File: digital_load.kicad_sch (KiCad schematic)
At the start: 0 parts

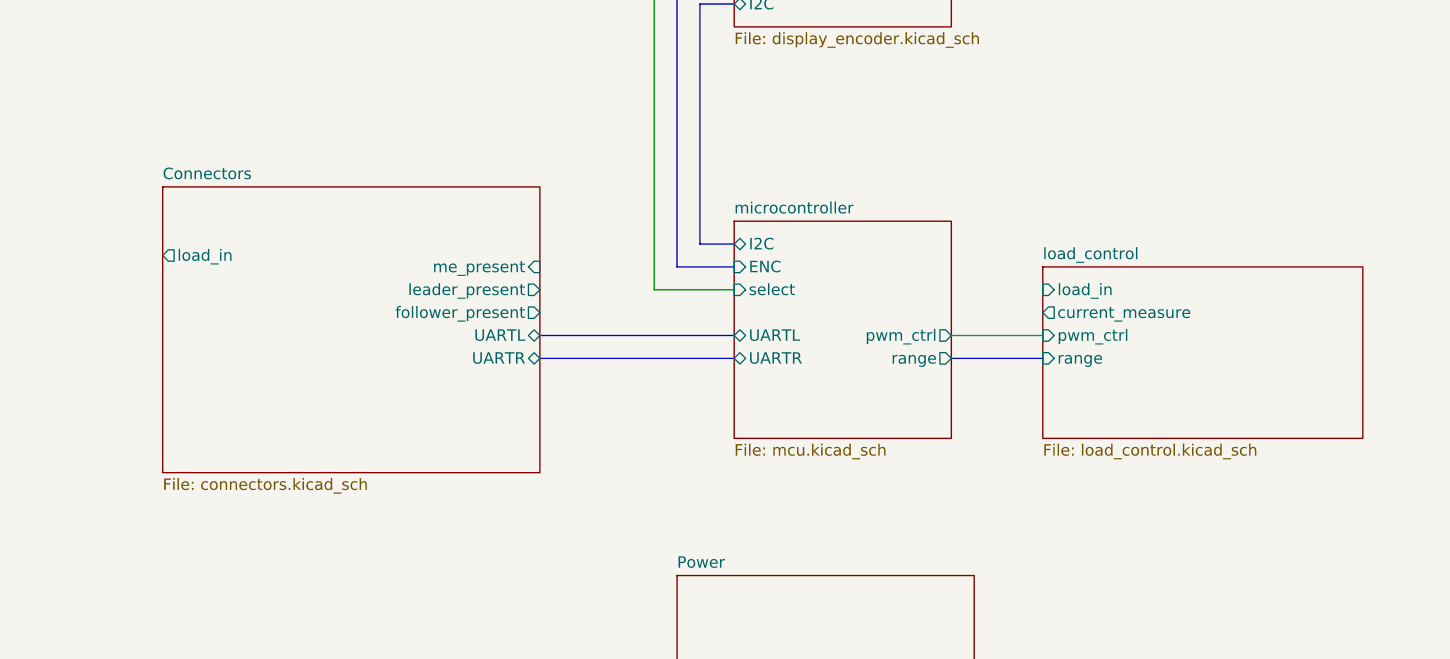
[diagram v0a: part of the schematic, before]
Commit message: Replace UART{R,L} with I2C
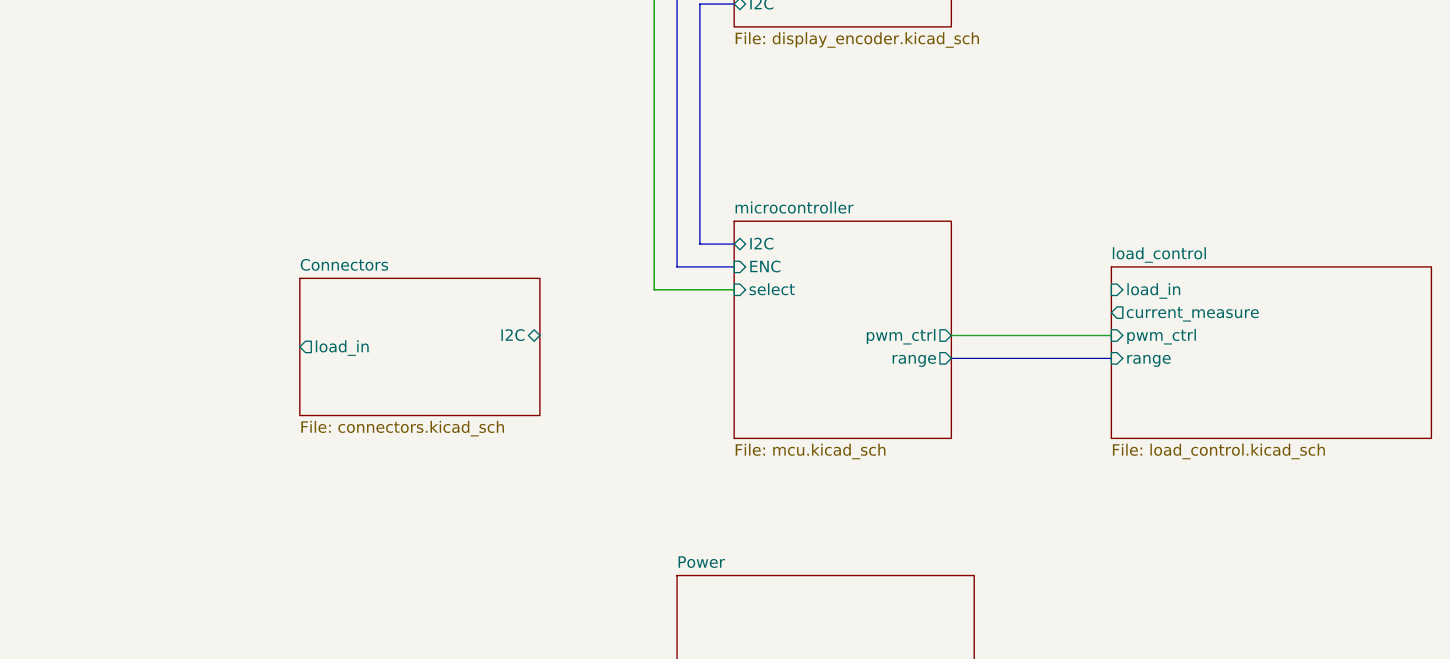
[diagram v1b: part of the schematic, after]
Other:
- sheet Connectors ports: added I2C; removed UARTL, UARTR, follower_present, leader_present, me_present
- sheet microcontroller ports: added none; removed UARTL, UARTR
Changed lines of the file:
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@@
 (kicad_sch (version 20211123) (generator eeschema)
   (paper "A4")
-  (bus (pts (xy 125.73 68.58) (xy 147.32 68.58))
-    (stroke (width 0) (type default) (color 0 0 0 0))
-  )
   (bus (pts (xy 143.51 29.21) (xy 143.51 55.88))
     (stroke (width 0) (type default) (color 0 0 0 0))
@@
     (stroke (width 0) (type default) (color 0 0 0 0))
   )
-  (wire (pts (xy 171.45 66.04) (xy 181.61 66.04))
+  (wire (pts (xy 171.45 66.04) (xy 189.23 66.04))
     (stroke (width 0) (type default) (color 0 0 0 0))
   )
@@
     (stroke (width 0) (type default) (color 0 0 0 0))
   )
-  (bus (pts (xy 125.73 66.04) (xy 147.32 66.04))
-    (stroke (width 0) (type default) (color 0 0 0 0))
-  )
   (bus (pts (xy 140.97 26.67) (xy 140.97 58.42))
     (stroke (width 0) (type default) (color 0 0 0 0))
@@
     (stroke (width 0) (type default) (color 0 0 0 0))
   )
-  (bus (pts (xy 171.45 68.58) (xy 181.61 68.58))
+  (bus (pts (xy 171.45 68.58) (xy 189.23 68.58))
     (stroke (width 0) (type default) (color 0 0 0 0))
   )
@@
       (effects (font (size 1.27 1.27)) (justify left))
     )
-    (pin "UARTR" bidirectional (at 147.32 68.58 180)
-      (effects (font (size 1.27 1.27)) (justify left))
-    )
-    (pin "UARTL" bidirectional (at 147.32 66.04 180)
-      (effects (font (size 1.27 1.27)) (justify left))
-    )
     (pin "ENC" input (at 147.32 58.42 180)
       (effects (font (size 1.27 1.27)) (justify left))
@@
     )
   )
-  (sheet (at 181.61 58.42) (size 35.56 19.05) (fields_autoplaced)
-    (stroke (width 0.1524) (type solid) (color 0 0 0 0))
-    (fill (color 0 0 0 0.0000))
-    (property "Sheet name" "load_control" (id 0) (at 181.61 57.7084 0)
-      (effects (font (size 1.27 1.27)) (justify left bottom))
-    )
-    (property "Sheet file" "load_control.kicad_sch" (id 1) (at 181.61 78.0546 0)
-      (effects (font (size 1.27 1.27)) (justify left top))
-    )
-    (pin "current_measure" output (at 181.61 63.5 180)
-      (effects (font (size 1.27 1.27)) (justify left))
-    )
-    (pin "pwm_ctrl" input (at 181.61 66.04 180)
-      (effects (font (size 1.27 1.27)) (justify left))
-    )
-    (pin "load_in" input (at 181.61 60.96 180)
-      (effects (font (size 1.27 1.27)) (justify left))
-    )
-    (pin "range" input (at 181.61 68.58 180)
-      (effects (font (size 1.27 1.27)) (justify left))
-    )
-  )
-  (sheet (at 83.82 49.53) (size 41.91 31.75) (fields_autoplaced)
-    (stroke (width 0.1524) (type solid) (color 0 0 0 0))
-    (fill (color 0 0 0 0.0000))
-    (property "Sheet name" "Connectors" (id 0) (at 83.82 48.8184 0)
-      (effects (font (size 1.27 1.27)) (justify left bottom))
-    )
-    (property "Sheet file" "connectors.kicad_sch" (id 1) (at 83.82 81.8646 0)
-      (effects (font (size 1.27 1.27)) (justify left top))
-    )
-    (pin "load_in" output (at 83.82 57.15 180)
-      (effects (font (size 1.27 1.27)) (justify left))
-    )
-    (pin "me_present" input (at 125.73 58.42 0)
-      (effects (font (size 1.27 1.27)) (justify right))
-    )
-    (pin "leader_present" output (at 125.73 60.96 0)
-      (effects (font (size 1.27 1.27)) (justify right))
-    )
-    (pin "follower_present" output (at 125.73 63.5 0)
-      (effects (font (size 1.27 1.27)) (justify right))
-    )
-    (pin "UARTL" bidirectional (at 125.73 66.04 0)
-      (effects (font (size 1.27 1.27)) (justify right))
-    )
-    (pin "UARTR" bidirectional (at 125.73 68.58 0)
+  (sheet (at 189.23 58.42) (size 35.56 19.05) (fields_autoplaced)
+    (stroke (width 0.1524) (type solid) (color 0 0 0 0))
+    (fill (color 0 0 0 0.0000))
+    (property "Sheet name" "load_control" (id 0) (at 189.23 57.7084 0)
+      (effects (font (size 1.27 1.27)) (justify left bottom))
+    )
+    (property "Sheet file" "load_control.kicad_sch" (id 1) (at 189.23 78.0546 0)
+      (effects (font (size 1.27 1.27)) (justify left top))
+    )
+    (pin "current_measure" output (at 189.23 63.5 180)
+      (effects (font (size 1.27 1.27)) (justify left))
+    )
+    (pin "pwm_ctrl" input (at 189.23 66.04 180)
+      (effects (font (size 1.27 1.27)) (justify left))
+    )
+    (pin "load_in" input (at 189.23 60.96 180)
+      (effects (font (size 1.27 1.27)) (justify left))
+    )
+    (pin "range" input (at 189.23 68.58 180)
+      (effects (font (size 1.27 1.27)) (justify left))
+    )
+  )
+  (sheet (at 99.06 59.69) (size 26.67 15.24) (fields_autoplaced)
+    (stroke (width 0.1524) (type solid) (color 0 0 0 0))
+    (fill (color 0 0 0 0.0000))
+    (property "Sheet name" "Connectors" (id 0) (at 99.06 58.9784 0)
+      (effects (font (size 1.27 1.27)) (justify left bottom))
+    )
+    (property "Sheet file" "connectors.kicad_sch" (id 1) (at 99.06 75.5146 0)
+      (effects (font (size 1.27 1.27)) (justify left top))
+    )
+    (pin "load_in" output (at 99.06 67.31 180)
+      (effects (font (size 1.27 1.27)) (justify left))
+    )
+    (pin "I2C" bidirectional (at 125.73 66.04 0)
       (effects (font (size 1.27 1.27)) (justify right))
     )
@@
       (reference "#PWR?") (unit 1) (value "GND") (footprint "")
     )
+    (path "/86919485-4d16-4938-9e70-3e52b129563d/a5037bfd-93d7-49d6-9695-06cd238a5eca"
+      (reference "#PWR?") (unit 1) (value "+3.3V") (footprint "")
+    )
+    (path "/f4f89a23-25ef-48cf-b1e7-482fc7d24406/bbb1dd21-e40d-4e60-94aa-207520d46274"
+      (reference "#PWR?") (unit 1) (value "+5V") (footprint "")
+    )
     (path "/3a4d7b94-8b26-4555-b396-f2e88aea5db3/dc7cb313-d8a8-40ad-b615-2421d40e41fc"
       (reference "#PWR?") (unit 1) (value "+3.3V") (footprint "")
     )
+    (path "/f4f89a23-25ef-48cf-b1e7-482fc7d24406/e16f3f10-89b9-4599-8444-89c5df9a6fca"
+      (reference "#PWR?") (unit 1) (value "GND") (footprint "")
+    )
     (path "/b9283ecb-6055-4d8e-90be-13b597248a91/047fbb72-cf84-4710-a4c8-84372e31468c"
       (reference "C20") (unit 1) (value "C") (footprint "Capacitor_SMD:C_0805_2012Metric")
@@
       (reference "Q23") (unit 1) (value "Q_NMOS_DGS") (footprint "Package_TO_SOT_SMD:SOT-23")
     )
+    (path "/86919485-4d16-4938-9e70-3e52b129563d/b8576b39-1899-434e-a216-d803d9a57b8b"
+      (reference "R10") (unit 1) (value "10k") (footprint "Resistor_SMD:R_0805_2012Metric")
+    )
+    (path "/86919485-4d16-4938-9e70-3e52b129563d/bfa347ee-29a1-4fa6-bd17-f85f8a9abc80"
+      (reference "R11") (unit 1) (value "10k") (footprint "Resistor_SMD:R_0805_2012Metric")
+    )
+    (path "/86919485-4d16-4938-9e70-3e52b129563d/1142d0b4-3f0c-400a-95f4-56b82d3f695d"
+      (reference "R12") (unit 1) (value "10k") (footprint "Resistor_SMD:R_0805_2012Metric")
+    )
     (path "/b9283ecb-6055-4d8e-90be-13b597248a91/1c61f331-fa92-48e1-9819-ab0be4ebf718"
       (reference "R20") (unit 1) (value "R_US") (footprint "Resistor_SMD:R_0805_2012Metric")
@@
       (reference "R?") (unit 1) (value "10k") (footprint "Resistor_SMD:R_0805_2012Metric")
     )
-    (path "/86919485-4d16-4938-9e70-3e52b129563d/b8576b39-1899-434e-a216-d803d9a57b8b"
-      (reference "R?") (unit 1) (value "10k") (footprint "Resistor_SMD:R_0805_2012Metric")
-    )

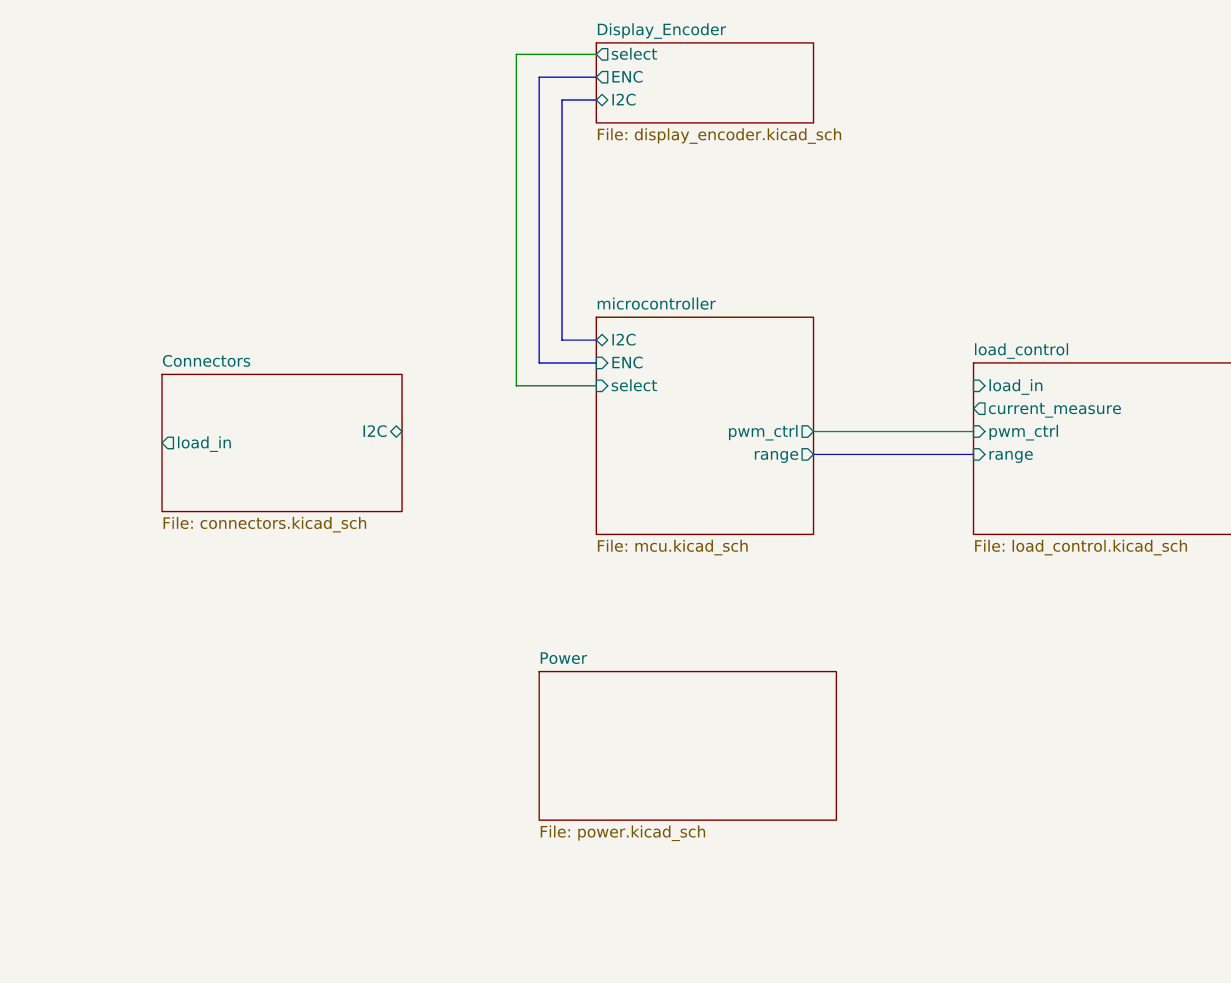
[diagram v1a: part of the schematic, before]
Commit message: Add voltage reference and voltage regulator
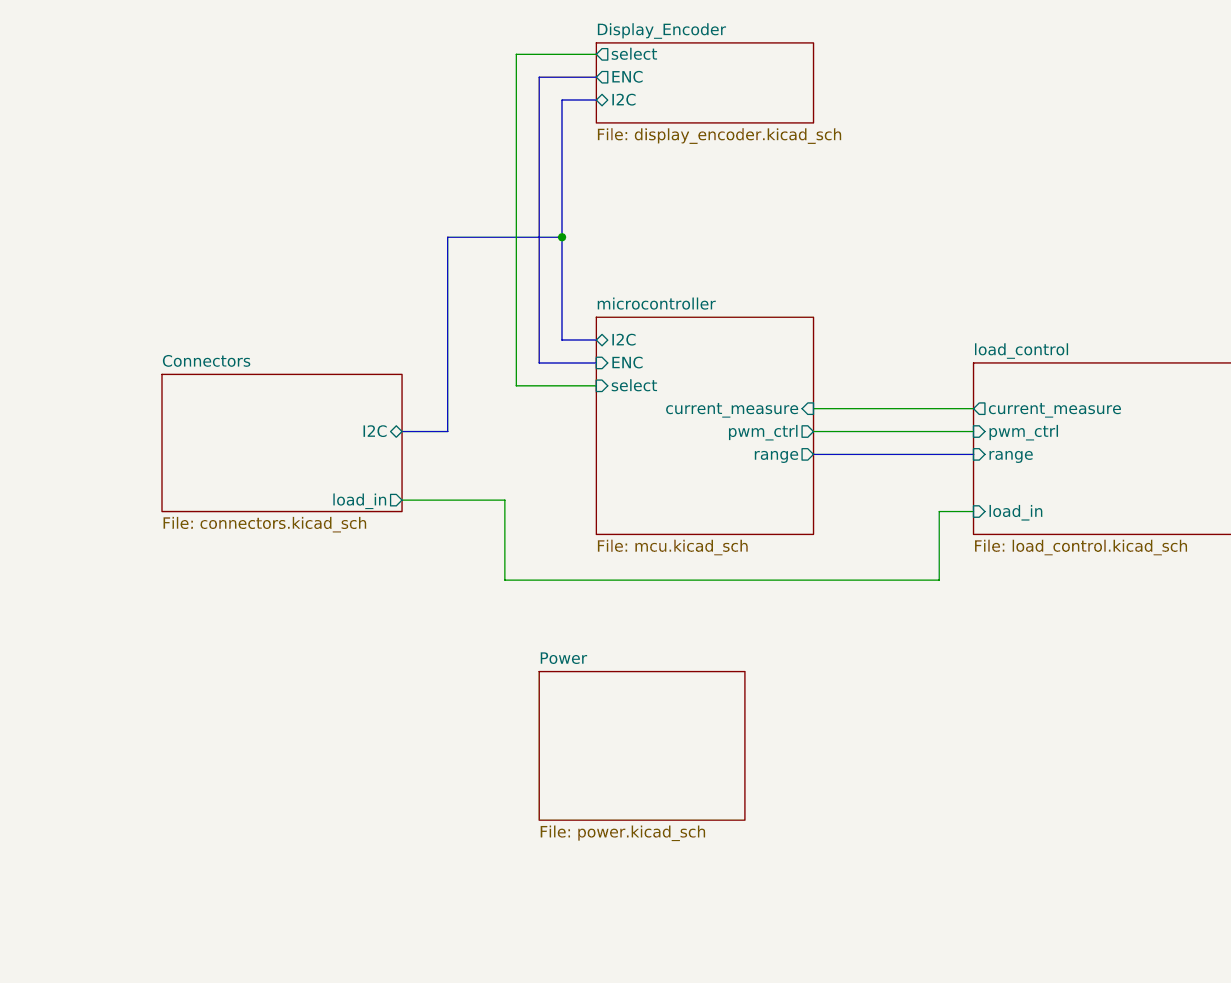
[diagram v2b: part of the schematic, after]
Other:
- sheet microcontroller ports: added current_measure; removed none

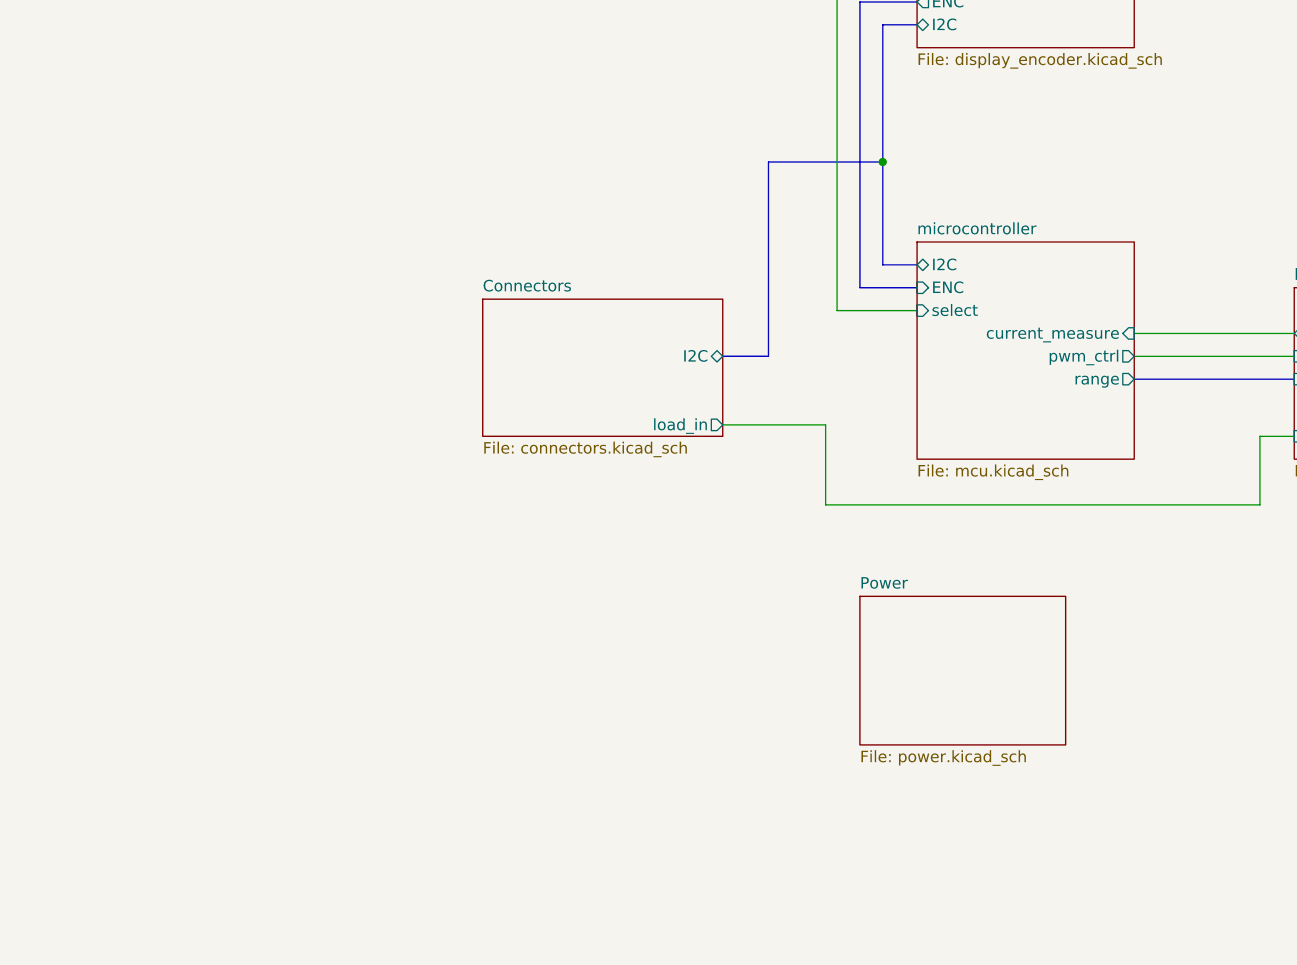
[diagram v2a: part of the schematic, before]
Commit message: Add uart usb controller
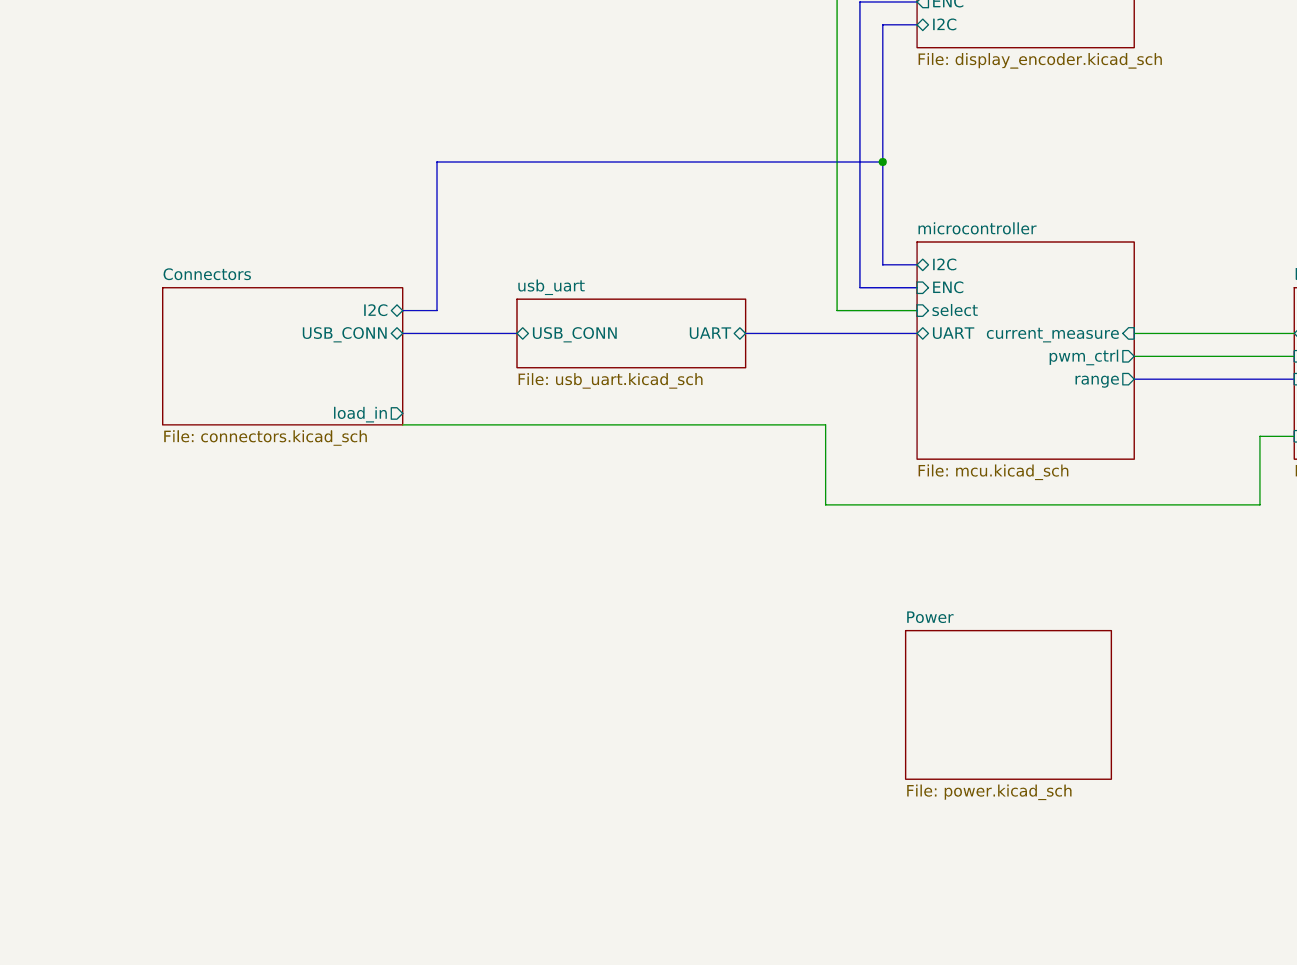
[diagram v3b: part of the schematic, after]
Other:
- added sheet usb_uart (usb_uart.kicad_sch)
- sheet Connectors ports: added USB_CONN; removed none
- sheet microcontroller ports: added UART; removed none
